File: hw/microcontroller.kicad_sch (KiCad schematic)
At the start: 12 parts

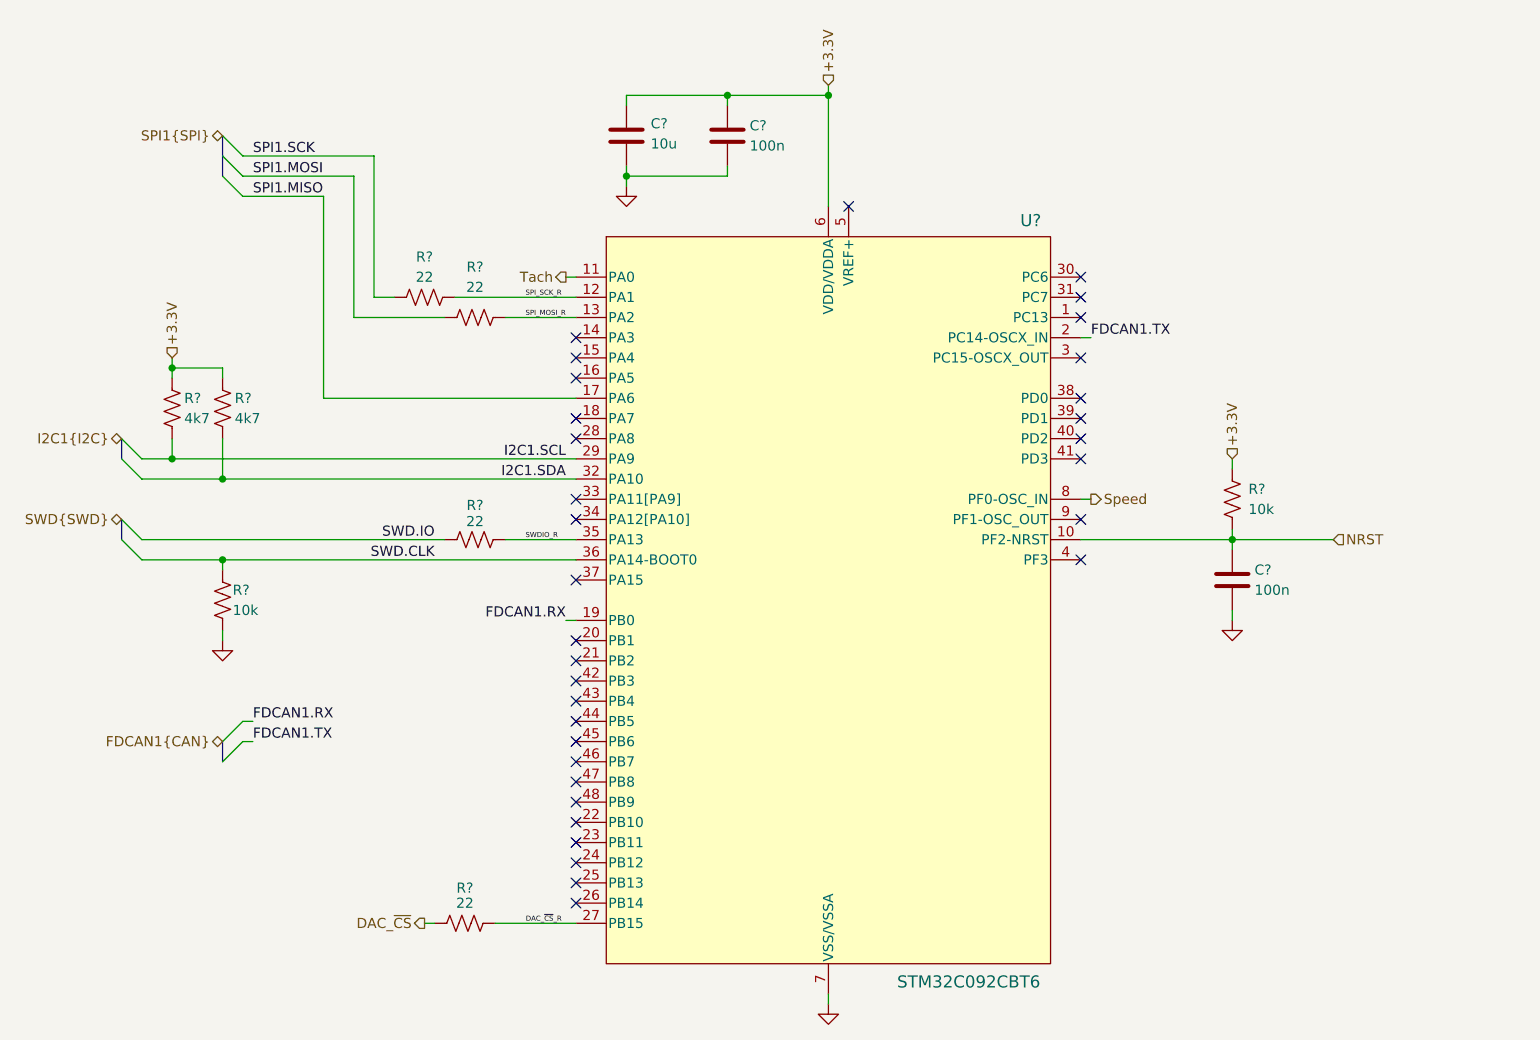
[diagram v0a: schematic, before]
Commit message: hw: clean up microcontroller schematic
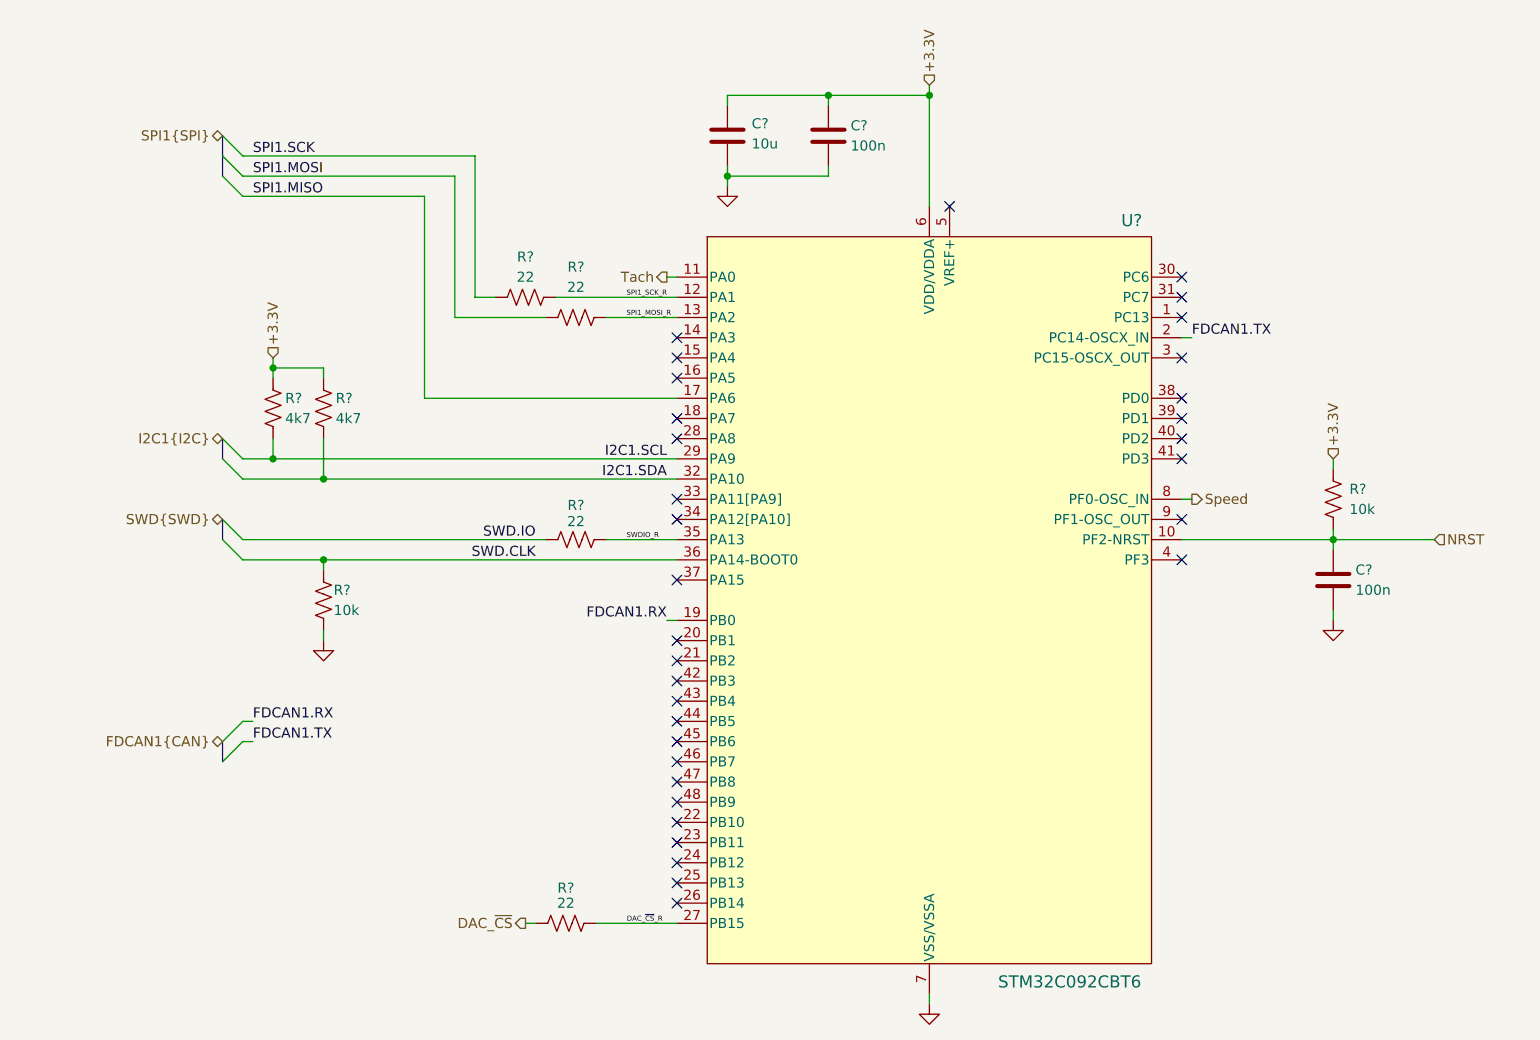
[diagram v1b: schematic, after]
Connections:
- net SPI_MOSI_R renamed SPI1_MOSI_R
- net SPI_SCK_R renamed SPI1_SCK_R
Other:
- moved on the sheet: C?, R?, U?

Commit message: hw: dac hierarchical sheet
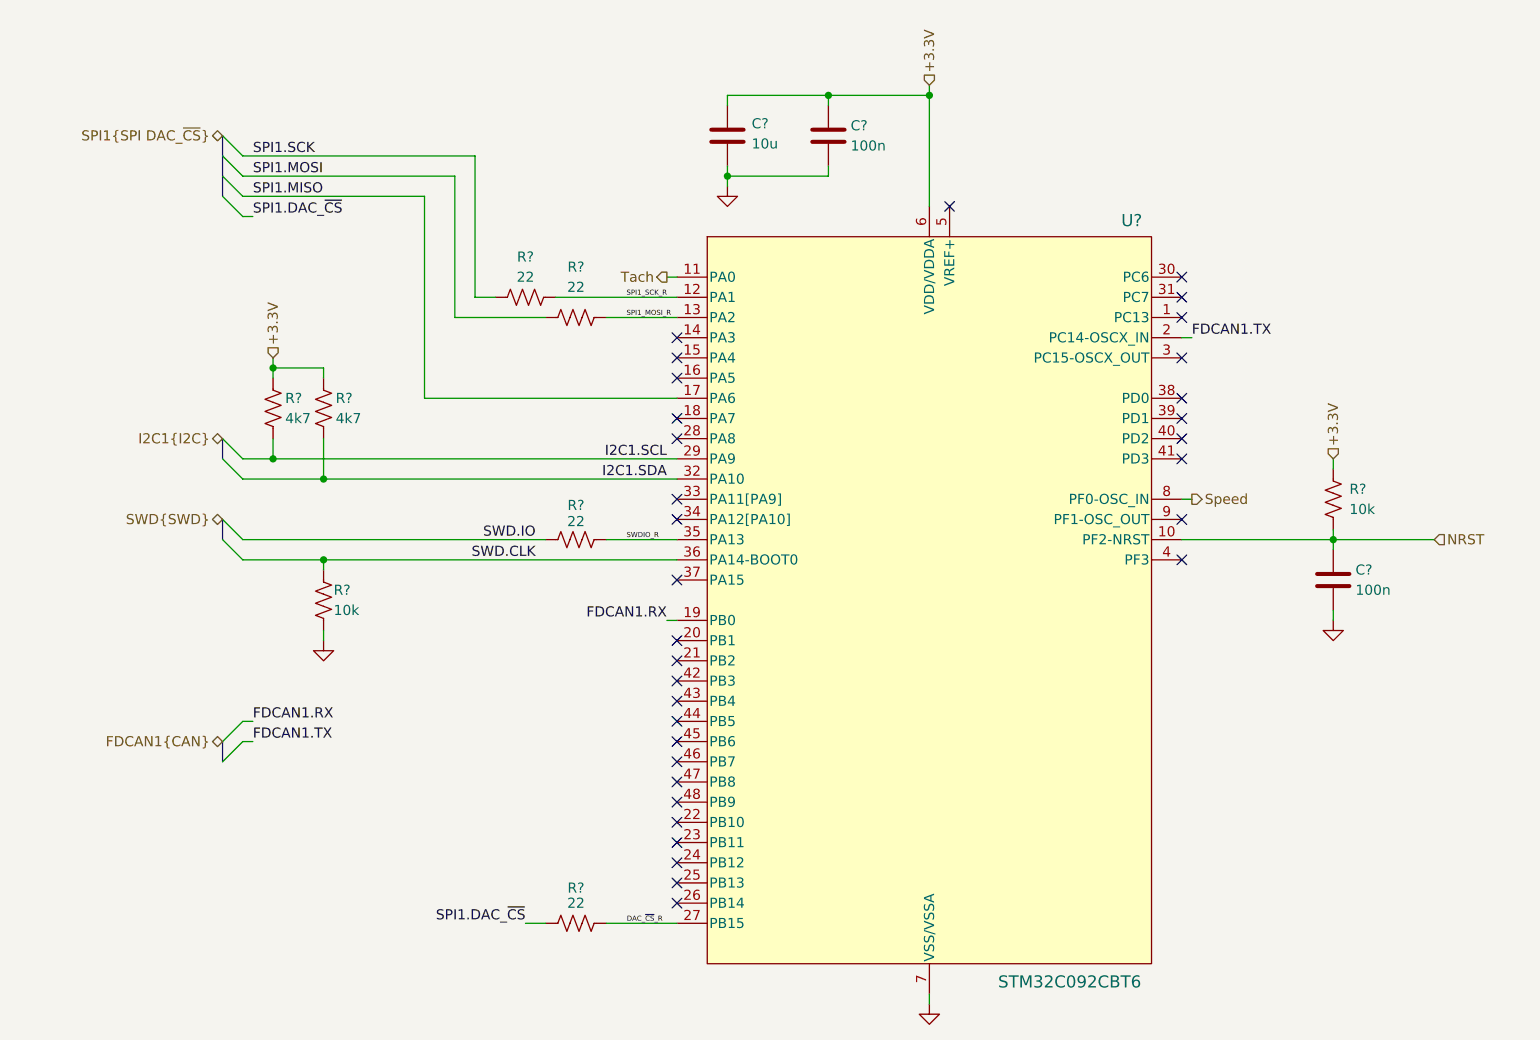
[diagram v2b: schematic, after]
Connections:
- net DAC_~{CS} renamed SPI1.DAC_~{CS}
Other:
- moved on the sheet: R?
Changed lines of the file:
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@@
+	)
+	(bus_entry
+		(at 38.1 45.72)
+		(size 2.54 2.54)
+		(stroke
+			(width 0)
+			(type default)
+		)
 	)
 	(bus_entry
@@
 	(wire
 		(pts
-			(xy 76.2 137.16) (xy 77.47 137.16)
-		)
-		(stroke
-			(width 0)
-			(type default)
-		)
-	)
-	(wire
-		(pts
 			(xy 44.45 66.04) (xy 44.45 67.31)
 		)
@@
 	(wire
 		(pts
+			(xy 40.64 48.26) (xy 41.91 48.26)
+		)
+		(stroke
+			(width 0)
+			(type default)
+		)
+	)
+	(wire
+		(pts
 			(xy 177.8 88.9) (xy 190.5 88.9)
 		)
@@
 	(wire
 		(pts
-			(xy 85.09 137.16) (xy 95.25 137.16)
-		)
-		(stroke
-			(width 0)
-			(type default)
-		)
-	)
-	(wire
-		(pts
 			(xy 158.75 63.5) (xy 160.02 63.5)
 		)
@@
 		)
 	)
+	(wire
+		(pts
+			(xy 76.2 137.16) (xy 78.74 137.16)
+		)
+		(stroke
+			(width 0)
+			(type default)
+		)
+	)
 	(bus
 		(pts
@@
 		)
 	)
+	(bus
+		(pts
+			(xy 38.1 43.18) (xy 38.1 45.72)
+		)
+		(stroke
+			(width 0)
+			(type default)
+		)
+	)
 	(wire
 		(pts
@@
 		(pts
 			(xy 63.5 45.72) (xy 63.5 71.12)
+		)
+		(stroke
+			(width 0)
+			(type default)
+		)
+	)
+	(wire
+		(pts
+			(xy 86.36 137.16) (xy 95.25 137.16)
 		)
 		(stroke
@@
 		)
 	)
+	(label "SPI1.DAC_~{CS}"
+		(at 41.91 48.26 0)
+		(effects
+			(font
+				(size 1.27 1.27)
+			)
+			(justify left bottom)
+		)
+	)
 	(label "FDCAN1.RX"
 		(at 93.98 99.06 180)
+		(effects
+			(font
+				(size 1.27 1.27)
+			)
+			(justify right bottom)
+		)
+	)
+	(label "SPI1.DAC_~{CS}"
+		(at 76.2 137.16 180)
 		(effects
 			(font
@@
 		)
 	)
-	(hierarchical_label "SPI1{SPI}"
+	(hierarchical_label "SPI1{SPI DAC_~{CS}}"
 		(shape bidirectional)
 		(at 38.1 38.1 180)
@@
 			)
 			(justify left)
-		)
-	)
-	(hierarchical_label "DAC_~{CS}"
-		(shape output)
-		(at 76.2 137.16 180)
-		(effects
-			(font
-				(size 1.27 1.27)
-			)
-			(justify right)
 		)
 	)
@@
 	(symbol
 		(lib_id "Device:R_US")
-		(at 81.28 137.16 90)
+		(at 82.55 137.16 90)
 		(unit 1)
 		(exclude_from_sim no)
@@
 		(dnp no)
 		(property "Reference" "R?"
-			(at 81.28 132.715 90)
+			(at 82.55 132.715 90)
 			(effects
 				(font
@@
 		)
 		(property "Value" "22"
-			(at 81.28 134.62 90)
+			(at 82.55 134.62 90)
 			(effects
 				(font
@@
 		)
 		(property "Footprint" "Resistor_SMD:R_0603_1608Metric"
-			(at 81.534 136.144 90)
+			(at 82.804 136.144 90)
 			(effects
 				(font
@@
 		)
 		(property "Datasheet" "~"
-			(at 81.28 137.16 0)
+			(at 82.55 137.16 0)
 			(effects
 				(font
@@
 		)
 		(property "Description" "Resistor, US symbol"
-			(at 81.28 137.16 0)
-			(effects
-				(font
+			(at 82.55 137.16 0)
+			(effects
+				(font

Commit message: hw: top level schematic
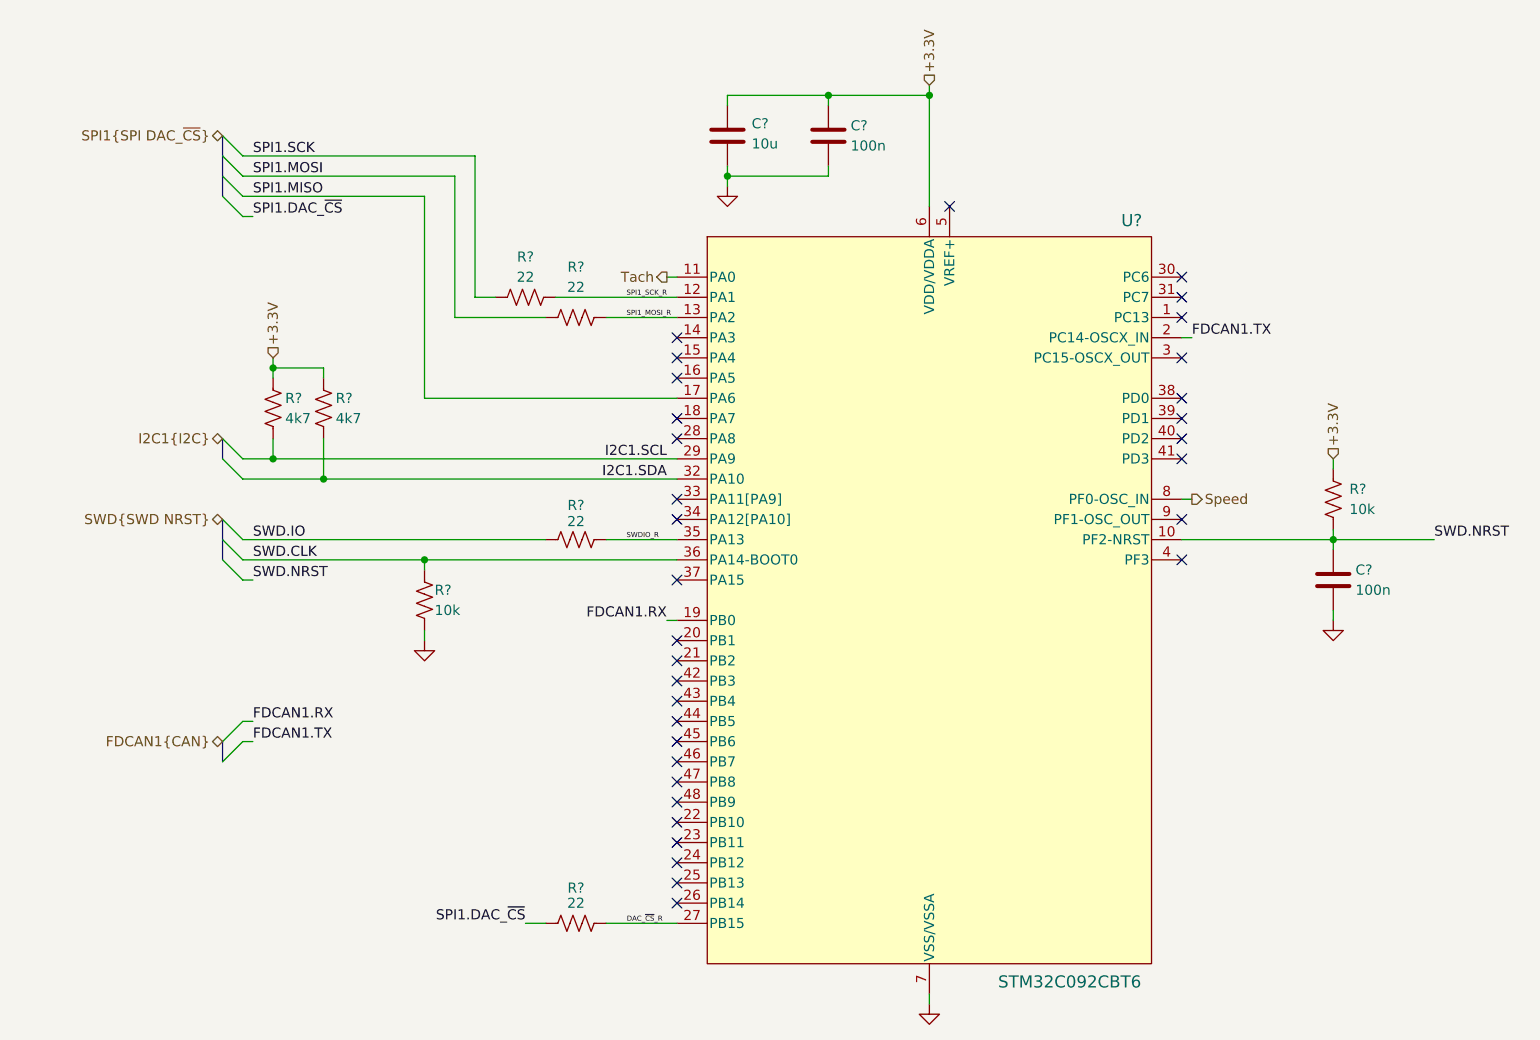
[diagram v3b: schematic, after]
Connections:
- net NRST renamed SWD.NRST
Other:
- moved on the sheet: R?
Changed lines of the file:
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@@
 	)
 	(junction
-		(at 50.8 91.44)
+		(at 63.5 91.44)
 		(diameter 0)
 		(color 0 0 0 0)
@@
 	)
 	(bus_entry
+		(at 38.1 91.44)
+		(size 2.54 2.54)
+		(stroke
+			(width 0)
+			(type default)
+		)
+	)
+	(bus_entry
 		(at 38.1 114.3)
 		(size 2.54 -2.54)
@@
 	(wire
 		(pts
-			(xy 40.64 91.44) (xy 50.8 91.44)
+			(xy 40.64 91.44) (xy 63.5 91.44)
 		)
 		(stroke
@@
 	(wire
 		(pts
+			(xy 63.5 91.44) (xy 95.25 91.44)
+		)
+		(stroke
+			(width 0)
+			(type default)
+		)
+	)
+	(wire
+		(pts
 			(xy 67.31 60.96) (xy 78.74 60.96)
 		)
@@
 	(wire
 		(pts
-			(xy 50.8 91.44) (xy 95.25 91.44)
-		)
-		(stroke
-			(width 0)
-			(type default)
-		)
-	)
-	(wire
-		(pts
 			(xy 40.64 78.74) (xy 44.45 78.74)
 		)
@@
 		)
 	)
+	(bus
+		(pts
+			(xy 38.1 88.9) (xy 38.1 91.44)
+		)
+		(stroke
+			(width 0)
+			(type default)
+		)
+	)
 	(wire
 		(pts
@@
 	(wire
 		(pts
-			(xy 50.8 91.44) (xy 50.8 92.71)
-		)
-		(stroke
-			(width 0)
-			(type default)
-		)
-	)
-	(wire
-		(pts
-			(xy 50.8 100.33) (xy 50.8 101.6)
+			(xy 63.5 91.44) (xy 63.5 92.71)
+		)
+		(stroke
+			(width 0)
+			(type default)
+		)
+	)
+	(wire
+		(pts
+			(xy 63.5 100.33) (xy 63.5 101.6)
 		)
 		(stroke
@@
 		(pts
 			(xy 93.98 99.06) (xy 95.25 99.06)
+		)
+		(stroke
+			(width 0)
+			(type default)
+		)
+	)
+	(wire
+		(pts
+			(xy 40.64 93.98) (xy 41.91 93.98)
 		)
 		(stroke
@@
 	)
 	(label "SWD.IO"
-		(at 77.47 88.9 180)
-		(effects
-			(font
-				(size 1.27 1.27)
-			)
-			(justify right bottom)
+		(at 41.91 88.9 0)
+		(effects
+			(font
+				(size 1.27 1.27)
+			)
+			(justify left bottom)
 		)
 	)
@@
 		)
 	)
+	(label "SWD.NRST"
+		(at 190.5 88.9 0)
+		(effects
+			(font
+				(size 1.27 1.27)
+			)
+			(justify left bottom)
+		)
+	)
 	(label "SWD.CLK"
-		(at 77.47 91.44 180)
-		(effects
-			(font
-				(size 1.27 1.27)
-			)
-			(justify right bottom)
+		(at 41.91 91.44 0)
+		(effects
+			(font
+				(size 1.27 1.27)
+			)
+			(justify left bottom)
 		)
 	)
@@
 		)
 	)
+	(label "SWD.NRST"
+		(at 41.91 93.98 0)
+		(effects
+			(font
+				(size 1.27 1.27)
+			)
+			(justify left bottom)
+		)
+	)
 	(label "FDCAN1.RX"
 		(at 93.98 99.06 180)
@@
 			)
 			(justify left bottom)
-		)
-	)
-	(hierarchical_label "NRST"
-		(shape input)
-		(at 190.5 88.9 0)
-		(effects
-			(font
-				(size 1.27 1.27)
-			)
-			(justify left)
 		)
 	)
@@
 		)
 	)
-	(hierarchical_label "SWD{SWD}"
+	(hierarchical_label "SWD{SWD NRST}"
 		(shape bidirectional)
 		(at 38.1 86.36 180)
@@
 	(symbol
 		(lib_id "power:GND")
-		(at 50.8 101.6 0)
+		(at 63.5 101.6 0)
 		(unit 1)
 		(exclude_from_sim no)
@@
 		(fields_autoplaced yes)
 		(property "Reference" "#PWR016"
-			(at 50.8 107.95 0)
+			(at 63.5 107.95 0)
 			(effects
 				(font
@@
 		)
 		(property "Value" "GND"
-			(at 50.8 106.68 0)
+			(at 63.5 106.68 0)
 			(effects
 				(font
@@
 		)
 		(property "Footprint" ""
-			(at 50.8 101.6 0)
+			(at 63.5 101.6 0)
 			(effects
 				(font
@@
 		)
 		(property "Datasheet" ""
-			(at 50.8 101.6 0)
+			(at 63.5 101.6 0)
 			(effects
 				(font
@@
 		)
 		(property "Description" "Power symbol creates a global label with name \"GND\" , ground"
-			(at 50.8 101.6 0)
+			(at 63.5 101.6 0)
 			(effects
 				(font
@@
 	(symbol
 		(lib_id "Device:R_US")
-		(at 50.8 96.52 0)
+		(at 63.5 96.52 0)
 		(unit 1)
 		(exclude_from_sim no)
@@
 		(dnp no)
 		(property "Reference" "R?"
-			(at 52.07 95.25 0)
+			(at 64.77 95.25 0)
 			(effects
 				(font
@@
 		)
 		(property "Value" "10k"
-			(at 52.07 97.79 0)
+			(at 64.77 97.79 0)
 			(effects
 				(font
@@
 		)
 		(property "Footprint" "Resistor_SMD:R_0603_1608Metric"
-			(at 51.816 96.774 90)
+			(at 64.516 96.774 90)
 			(effects
 				(font
@@
 		)
 		(property "Datasheet" "~"
-			(at 50.8 96.52 0)
+			(at 63.5 96.52 0)
 			(effects
 				(font
@@
 		)
 		(property "Description" "Resistor, US symbol"
-			(at 50.8 96.52 0)
-			(effects
-				(font
+			(at 63.5 96.52 0)
+			(effects
+				(font

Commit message: hw: erc: can
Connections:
- net FDCAN1.RX renamed CAN1.RX
- net FDCAN1.TX renamed CAN1.TX
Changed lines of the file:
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@@
 	(generator_version "9.0")
 	(paper "A4")
-	(bus_alias "CAN"
+	(bus_alias "CAN_IF"
 		(members "TX" "RX")
 	)
@@
 		)
 	)
-	(label "FDCAN1.TX"
+	(label "CAN1.TX"
 		(at 41.91 114.3 0)
 		(effects
@@
 		)
 	)
-	(label "FDCAN1.RX"
+	(label "CAN1.RX"
 		(at 93.98 99.06 180)
 		(effects
@@
 		)
 	)
-	(label "FDCAN1.RX"
+	(label "CAN1.RX"
 		(at 41.91 111.76 0)
 		(effects
@@
 		)
 	)
-	(label "FDCAN1.TX"
+	(label "CAN1.TX"
 		(at 160.02 63.5 0)
 		(effects
@@
 		)
 	)
-	(hierarchical_label "FDCAN1{CAN}"
+	(hierarchical_label "CAN1{CAN_IF}"
 		(shape bidirectional)
 		(at 38.1 114.3 180)
